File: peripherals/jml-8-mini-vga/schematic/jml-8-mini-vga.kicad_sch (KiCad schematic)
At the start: 14 parts, among them J1 VGA, J2 Z80, U1 Tang Nano 9K, U2 74LVC4245A, U3 74LVC4245A, X1 25.175MHz

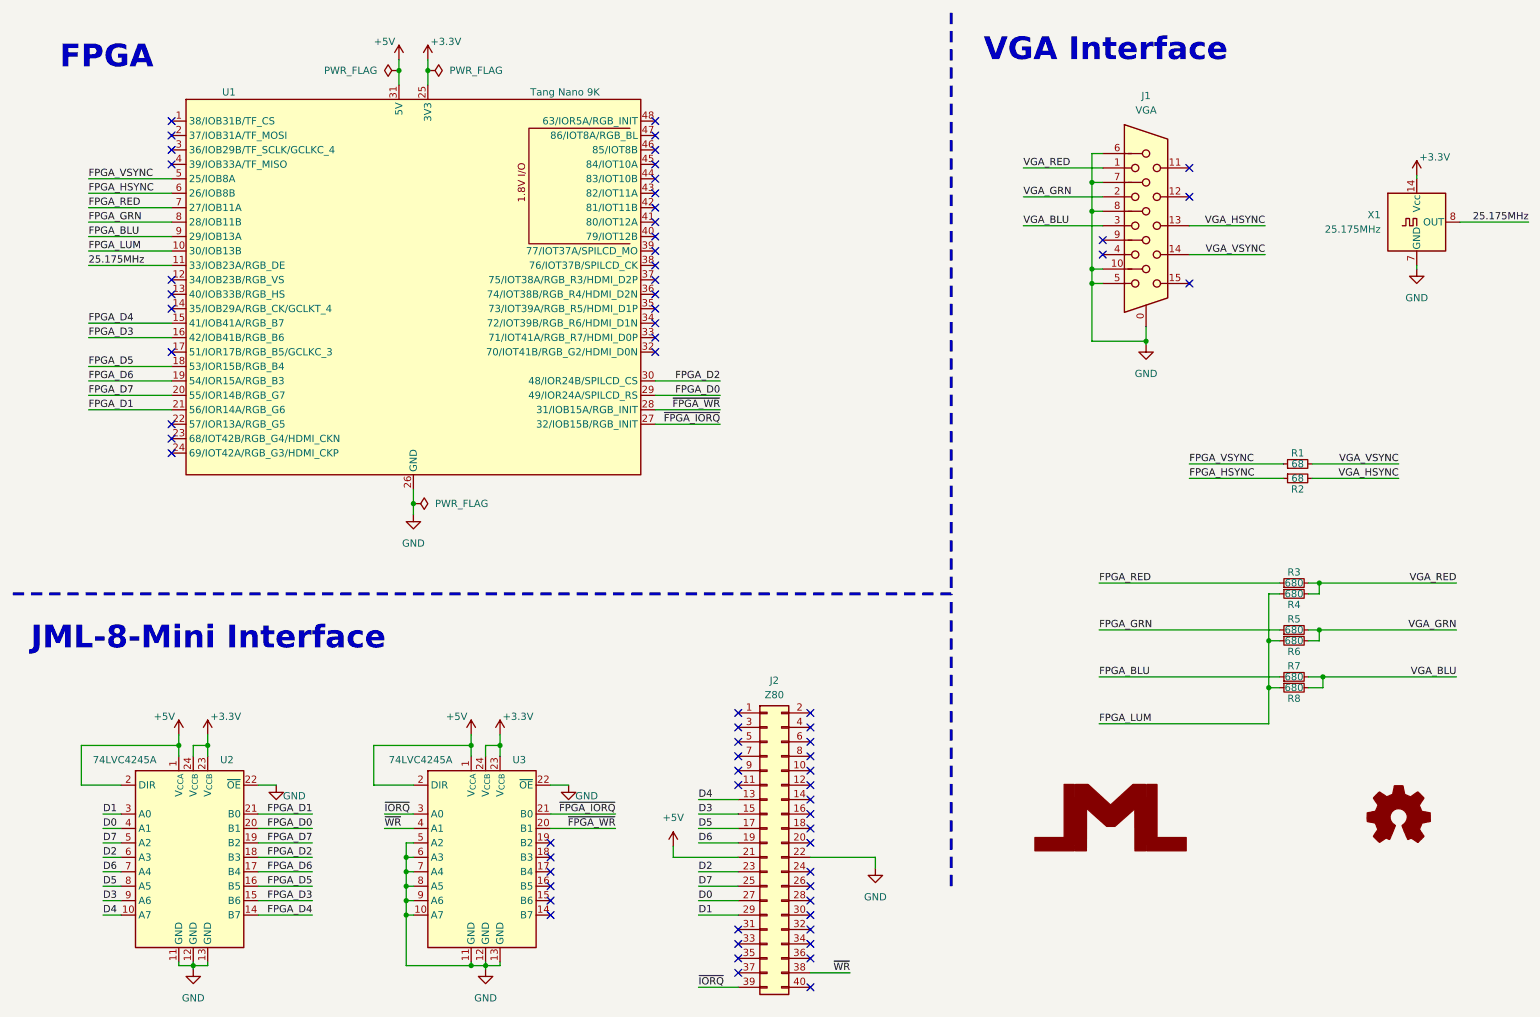
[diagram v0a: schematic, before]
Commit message: add address decoding circuitry, regenerate gerbers
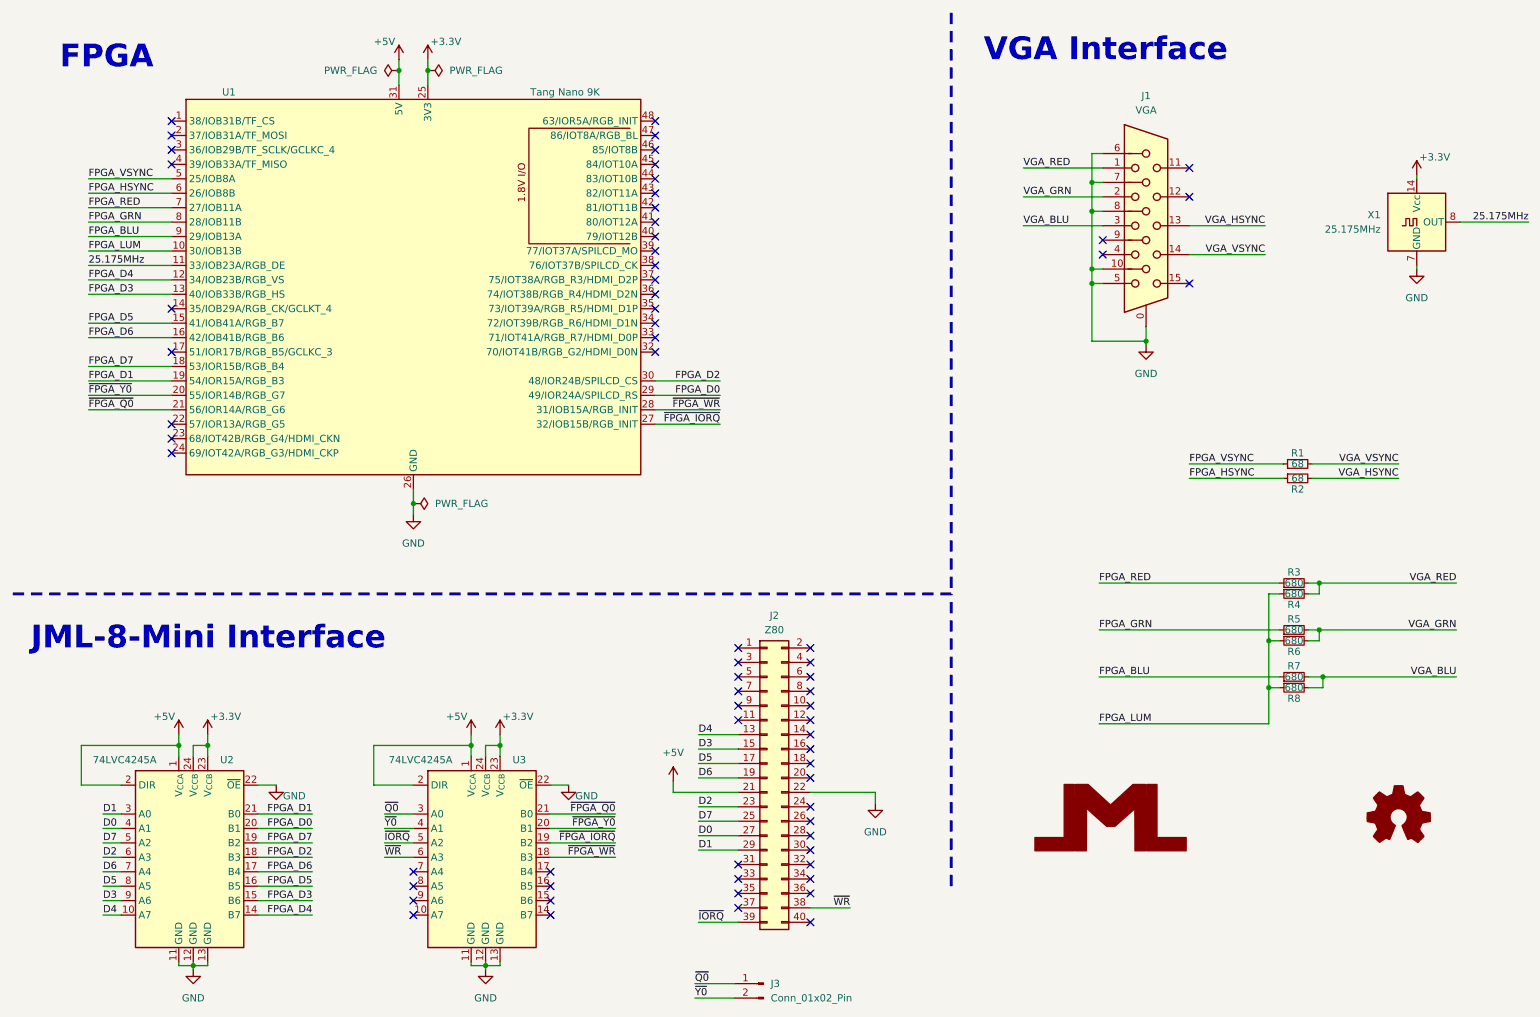
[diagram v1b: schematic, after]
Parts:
- added J3: Conn_01x02_Pin, Connector_PinHeader_2.54mm:PinHeader_1x02_P2.54mm_Vertical, symbol Connector:Conn_01x02_Pin
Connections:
- net FPGA_D1: now also U1.19 (54/IOR15A/RGB_B3); no longer U1.21 (56/IOR14A/RGB_G6)
- net FPGA_D3: now also U1.13 (40/IOB33B/RGB_HS); no longer U1.16 (42/IOB41B/RGB_B6)
- net FPGA_D4: now also U1.12 (34/IOB23B/RGB_VS); no longer U1.15 (41/IOB41A/RGB_B7)
- net FPGA_D5: now also U1.15 (41/IOB41A/RGB_B7); no longer U1.18 (53/IOR15B/RGB_B4)
- net FPGA_D6: now also U1.16 (42/IOB41B/RGB_B6); no longer U1.19 (54/IOR15A/RGB_B3)
- net FPGA_D7: now also U1.18 (53/IOR15B/RGB_B4); no longer U1.20 (55/IOR14B/RGB_G7)
- net GND: no longer U3.10 (A7), U3.5 (A2), U3.6 (A3), U3.7 (A4), U3.8 (A5), U3.9 (A6)
- net ~{FPGA_IORQ}: now also U3.19 (B2); no longer U3.21 (B0)
- net ~{FPGA_WR}: now also U3.18 (B3); no longer U3.20 (B1)
- net ~{IORQ}: now also U3.5 (A2); no longer U3.3 (A0)
- net ~{WR}: now also U3.6 (A3); no longer U3.4 (A1)
- new net ~{FPGA_Q0}: U1.21 (56/IOR14A/RGB_G6), U3.21 (B0)
- new net ~{FPGA_Y0}: U1.20 (55/IOR14B/RGB_G7), U3.20 (B1)
- new net ~{Q0}: J3.1 (Pin_1), U3.3 (A0)
- new net ~{Y0}: J3.2 (Pin_2), U3.4 (A1)
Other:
- moved on the sheet: J2
